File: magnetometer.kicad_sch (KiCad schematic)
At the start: 0 parts

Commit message: Initial component symbol placement
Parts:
- added U12: TMAG5273B1QDBVR, Library:SOT-23-6_L2.9-W1.6-P0.95-LS2.8-BL, symbol Library:TMAG5273B1QDBVR
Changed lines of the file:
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@@
 	(generator_version "9.0")
 	(paper "A4")
+	(symbol
+		(lib_id "Library:TMAG5273B1QDBVR")
+		(at 139.7 99.06 0)
+		(unit 1)
+		(exclude_from_sim no)
+		(in_bom yes)
+		(on_board yes)
+		(dnp no)
+		(fields_autoplaced yes)
+		(property "Reference" "U12"
+			(at 139.7 88.9 0)
+			(effects
+				(font
+					(size 1.27 1.27)
+				)
+			)
+		)
+		(property "Value" "TMAG5273B1QDBVR"
+			(at 139.7 91.44 0)
+			(effects
+				(font
+					(size 1.27 1.27)
+				)
+			)
+		)
+		(property "Footprint" "Library:SOT-23-6_L2.9-W1.6-P0.95-LS2.8-BL"
+			(at 139.7 109.22 0)
+			(effects
+				(font
+					(size 1.27 1.27)
+				)
+				(hide yes)
+			)
+		)
+		(property "Datasheet" "https://www.lcsc.com/datasheet/C7500517.pdf"
+			(at 139.7 111.76 0)
+			(effects
+				(font
+					(size 1.27 1.27)
+				)
+				(hide yes)
+			)
+		)
+		(property "Description" ""
+			(at 139.7 99.06 0)
+			(effects
+				(font
+					(size 1.27 1.27)
+				)
+				(hide yes)
+			)
+		)
+		(property "Manufacturer" "TI(德州仪器)"
+			(at 139.7 114.3 0)
+			(effects
+				(font
+					(size 1.27 1.27)
+				)
+				(hide yes)
+			)
+		)
+		(property "MPN" "TMAG5273B1QDBVR"
+			(at 139.7 116.84 0)
+			(effects
+				(font
+					(size 1.27 1.27)
+				)
+				(hide yes)
+			)
+		)
+		(property "LCSC Part" "C7500517"
+			(at 139.7 119.38 0)
+			(effects
+				(font
+					(size 1.27 1.27)
+				)
+				(hide yes)
+			)
+		)
+		(pin "2"
+		)
+		(pin "4"
+		)
+		(pin "3"
+		)
+		(pin "5"
+		)
+		(pin "1"
+		)
+		(pin "6"
+		)
+		(instances
+			(project ""
+				(path "/6af311bf-2fb1-446c-8c7e-7c930a463809/6c3ed190-5d43-4c7e-96d7-301ae7e00faf"
+					(reference "U12")
+					(unit 1)
+				)
+				(path "/6af311bf-2fb1-446c-8c7e-7c930a463809/9d43ef18-89de-4818-bc23-6c030e7dd232"
+					(reference "U14")
+					(unit 1)
+				)
+			)
+		)
+	)
 )

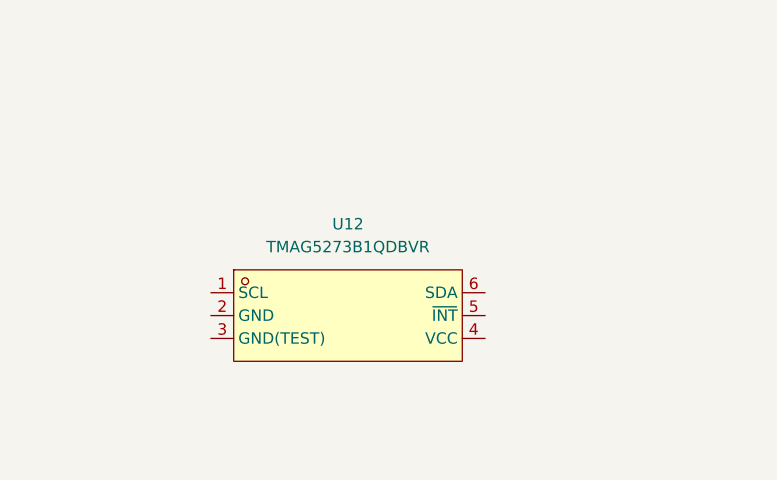
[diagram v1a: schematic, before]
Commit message: MCU implementation start Still needs component schematic checks & component integration with MCU
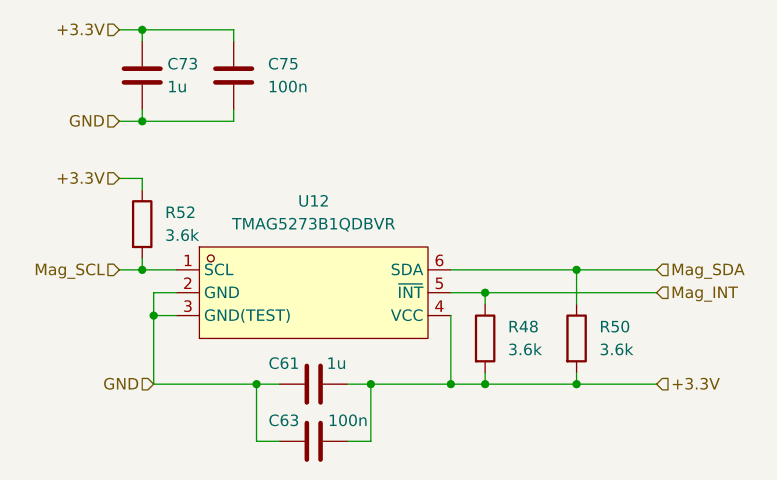
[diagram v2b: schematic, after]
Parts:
- added C61, C73: 1u, symbol Device:C
- added C63, C75: 100n, symbol Device:C
- added R48, R50, R52: 3.6k, symbol Device:R
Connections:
- net Mag_SCL: now reaches U12.1 (SCL)
- net Mag_SCL: now also R52.2
- net GND: now reaches U12.2 (GND)
- net GND: now also U12.3 (GND(TEST)), C61.1, C63.1, C73.2, C75.2
- net +3.3V: now reaches U12.4 (VCC)
- net +3.3V: now also C61.2, C63.2, C73.1, C75.1, R48.2, R50.2, R52.1
- net Mag_INT: now reaches U12.5 (~{INT})
- net Mag_INT: now also R48.1
- net Mag_SDA: now reaches U12.6 (SDA)
- net Mag_SDA: now also R50.1
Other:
- moved on the sheet: U12
